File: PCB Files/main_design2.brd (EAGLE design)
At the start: 50.7 x 26.6 mm, 41 parts, among them IC1 7805TV, IC2 MCP73831

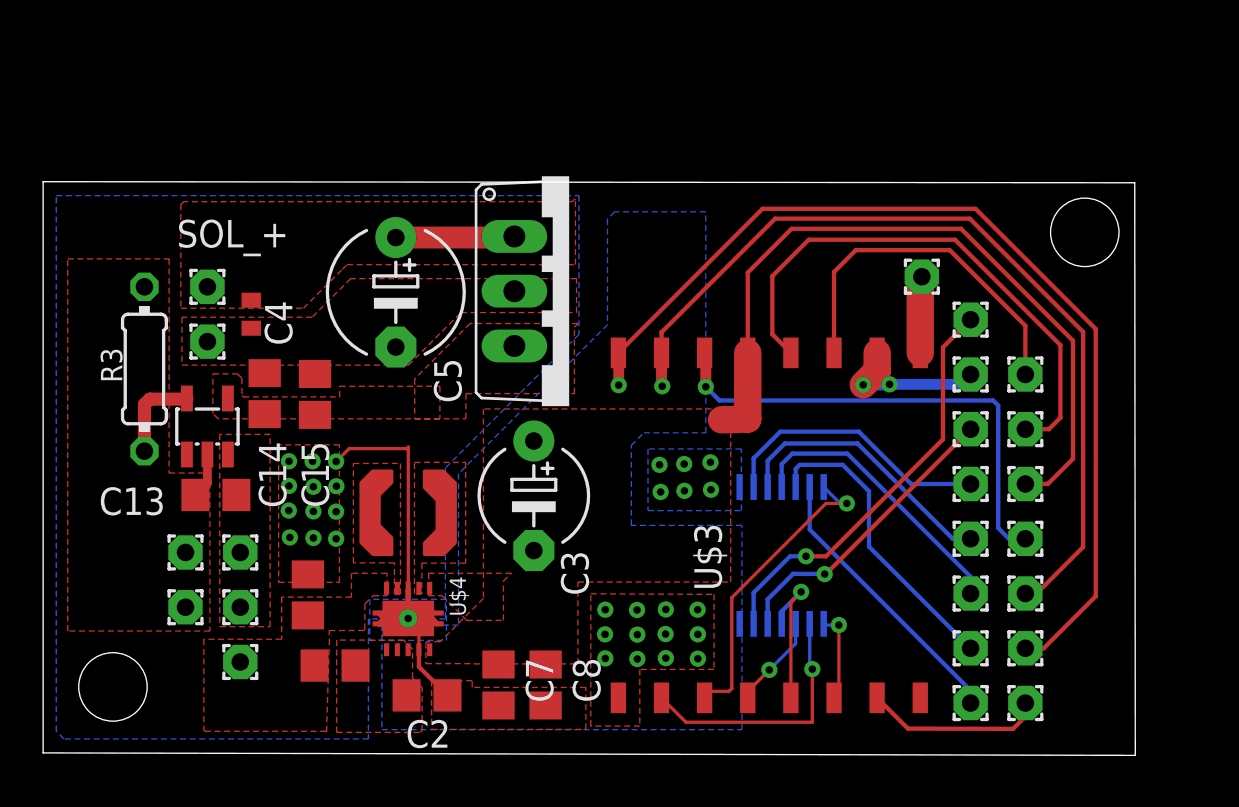
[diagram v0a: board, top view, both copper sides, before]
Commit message: 9.19 new PCB and code is working. currently set to standard power, not H-power versions of RFM69.
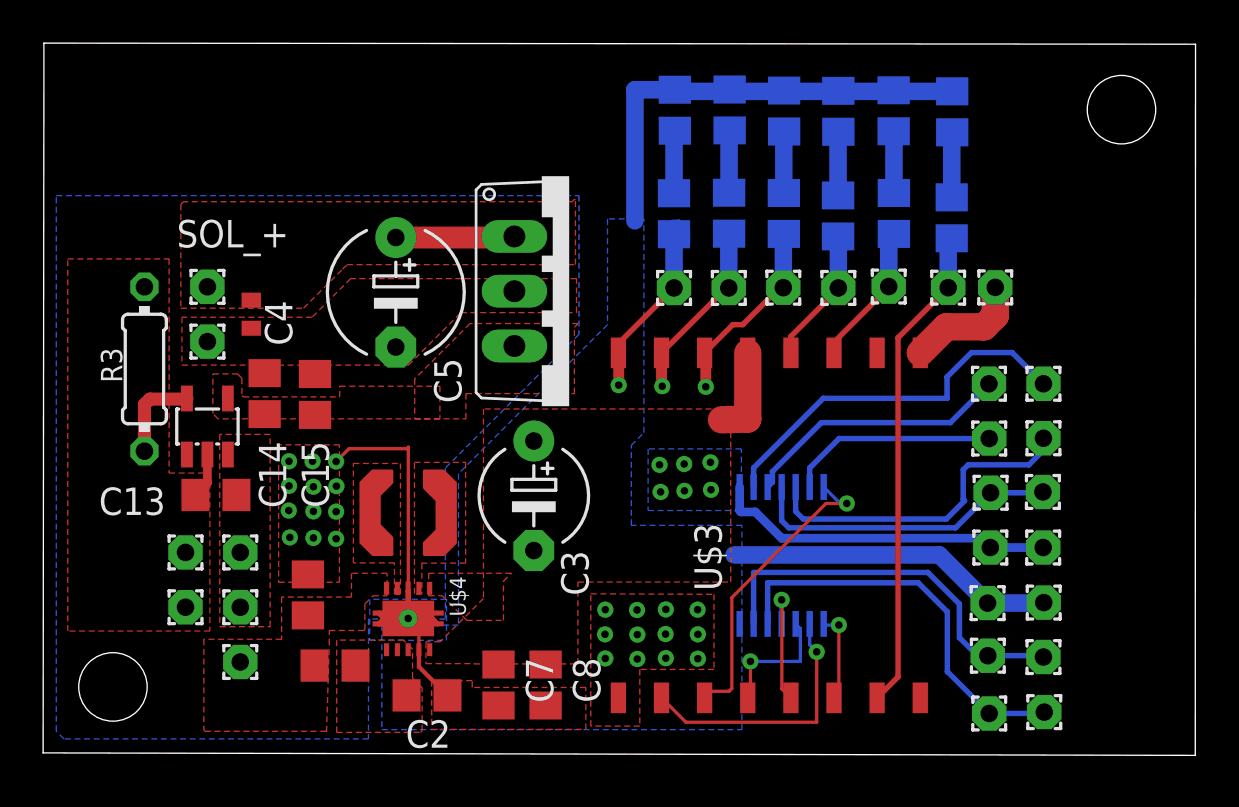
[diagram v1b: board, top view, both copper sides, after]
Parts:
- added DIO0_P, DIO1_P, DIO2_P, DIO3_P, DIO4_P, DIO5_P, KIT3_1, KIT3_2, KIT3_3, KIT3_4, KIT3_5: (no value), wirepad:1,6/0,8
- added DIO0_RES, DIO1_RES, DIO2_RES, DIO3_RES, DIO4_RES, DIO5_RES: (no value), rcl:R0805
- DIO0, DIO1, DIO2, DIO3, DIO4, DIO5: device wirepad:1,6/0,8 -> rcl:R0805
- moved DIO2 29.8 mm to (23.5, 99.8), flipped to the bottom, turned to 270 degrees
- moved DIO5 27.6 mm to (36.3, 99.7), flipped to the bottom, turned to 270 degrees
- moved DIO1 26.3 mm to (26.0, 99.8), flipped to the bottom, turned to 270 degrees
- moved DIO0 22.8 mm to (28.5, 99.7), flipped to the bottom, turned to 270 degrees
- moved DIO4 17.1 mm to (31.0, 99.7), flipped to the bottom, turned to 270 degrees
- moved ICSPDAT 15.6 mm to (38.0, 74.5)
- moved DIO3 13.7 mm to (33.6, 99.7), flipped to the bottom, turned to 270 degrees
- moved ICSPCLK 13.2 mm to (38.0, 71.8)
- moved RC4 12.3 mm to (38.0, 84.5), turned to 180 degrees
- moved GND7 10.6 mm to (38.0, 76.9)
- moved RC5 10.3 mm to (40.6, 84.5), turned to 180 degrees
- moved RA4 7.24 mm to (38.0, 87.1), turned to 180 degrees
- moved RA5 5.75 mm to (40.6, 87.1), turned to 180 degrees
- moved MCLR 4.76 mm to (38.1, 82.0), turned to 180 degrees
- moved ANT 3.44 mm to (38.3, 91.5)
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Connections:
- removed net N$18: DIO3.1, U$3.DIO3
- new net N$11: DIO5.2, DIO5_RES.1
- new net N$23: DIO4.2, DIO4_RES.1
- new net N$24: DIO3.2, DIO3_RES.1
- new net N$25: DIO0.2, DIO0_RES.1
- new net N$26: DIO2.2, DIO2_RES.1
- new net N$28: DIO3_P.1, DIO3_RES.2, U$3.DIO3
- new net N$5: DIO1.2, DIO1_RES.1
- net GND: now also DIO0.1, DIO1.1, DIO2.1, DIO3.1, DIO4.1, DIO5.1, KIT3_3.1
- net N$12: now also KIT3_5.1
- net N$13: now also KIT3_4.1
- net N$14: now also KIT3_1.1
- net N$15: now also DIO1_P.1, DIO1_RES.2; no longer DIO1.1
- net N$16: now also DIO0_P.1, DIO0_RES.2; no longer DIO0.1
- net N$17: now also DIO4_P.1, DIO4_RES.2; no longer DIO4.1
- net N$20: now also DIO5_P.1, DIO5_RES.2; no longer DIO5.1
- net N$9: now also DIO2_P.1, DIO2_RES.2; no longer DIO2.1
- net VOUT: now also KIT3_2.1
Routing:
- net N$9: track 45.4 -> 9.46 mm
- net N$15: track 40.0 -> 8.47 mm
- net GND: track 29.9 -> 59.1 mm, vias 26 -> 24
- net N$17: track 25.2 -> 6.34 mm
- net N$18: track 16.8 -> 0.00 mm
- net N$20: track 8.33 -> 22.7 mm
- net VOUT: track 34.3 -> 20.2 mm
- net N$16: track 22.7 -> 9.00 mm
- net N$28: track 0.00 -> 6.67 mm
- net N$12: track 13.8 -> 18.9 mm, vias 1 -> 0
- net N$6: track 12.9 -> 17.7 mm
- net N$8: track 13.1 -> 9.77 mm
- net N$11: track 0.00 -> 3.03 mm
- net N$23: track 0.00 -> 2.96 mm
- net N$26: track 0.00 -> 2.92 mm
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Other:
- board size 50.7 x 26.6 mm -> 53.4 x 33 mm
